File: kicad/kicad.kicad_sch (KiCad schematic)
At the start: 19 parts, among them J1 12V_IN, J2 MOTOR_POLOLU_3039, J3 NUCLEO_G0B1RE_IF, J4 CAN, Q1 IRLZ44NPBF, U1 TC4427ACPA, U2 INA180A1IDBVR, U3 TCAN332DR

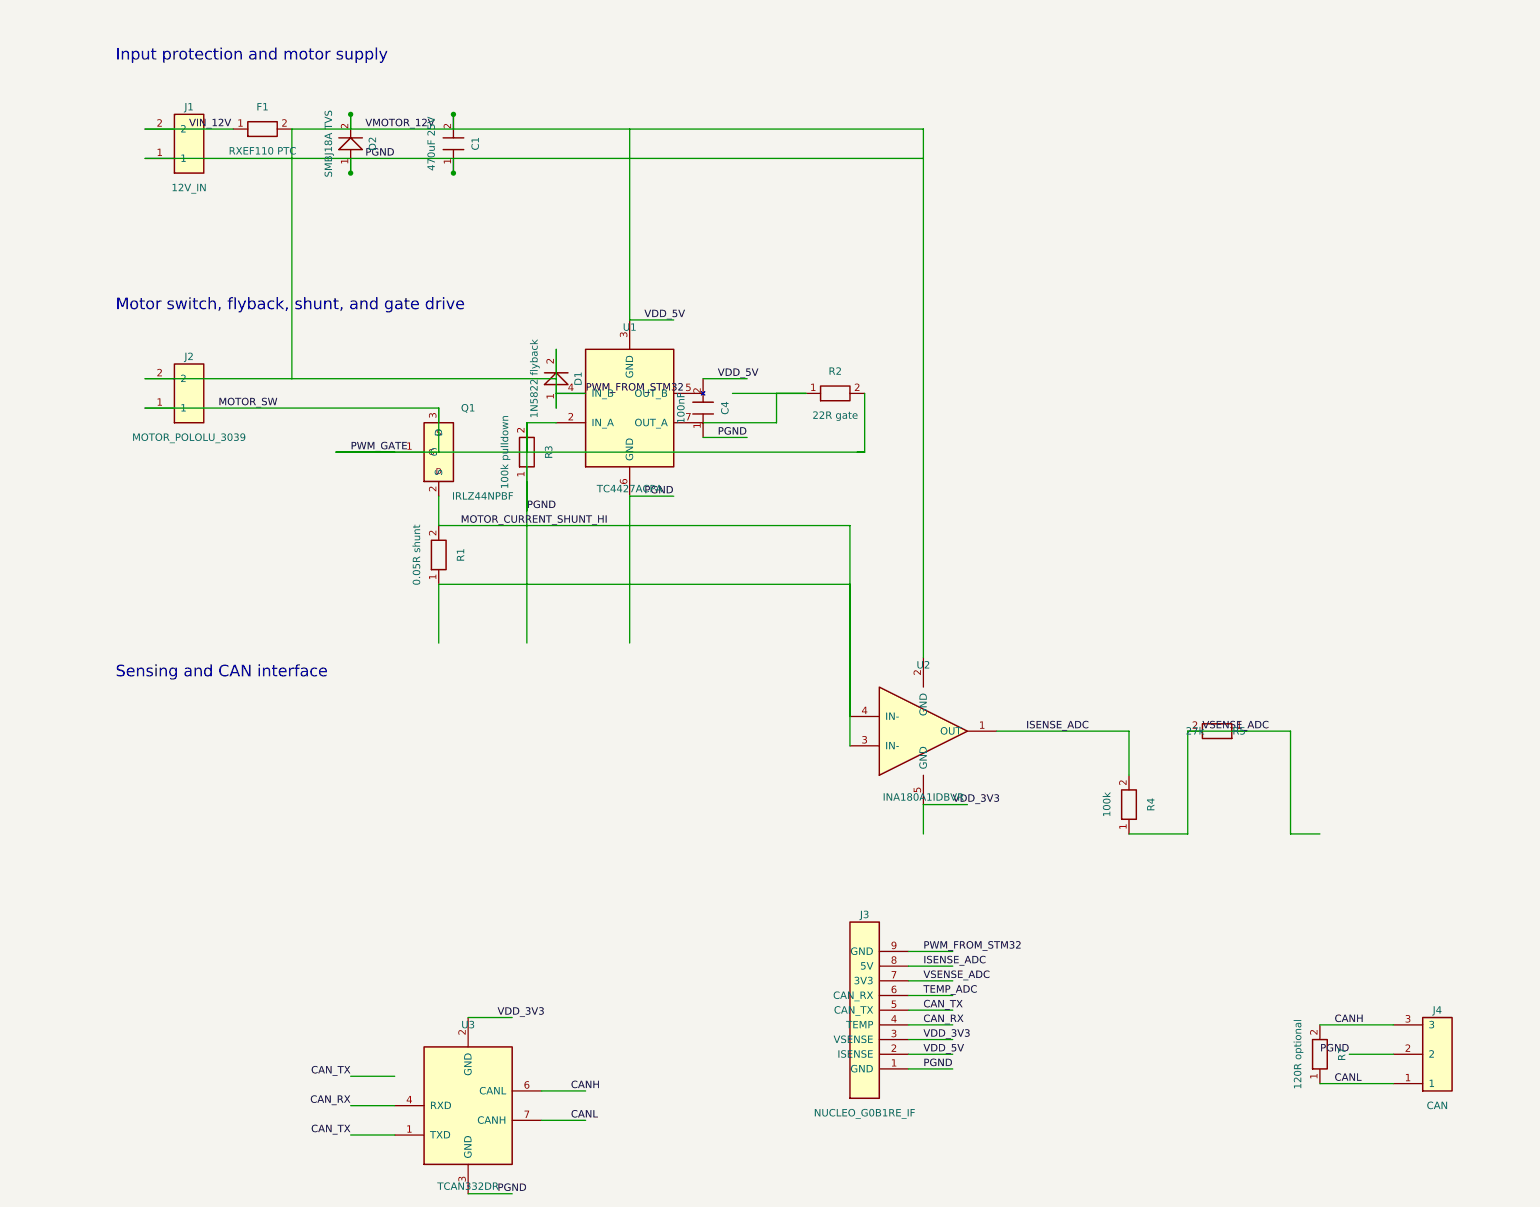
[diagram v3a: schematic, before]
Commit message: Finish schematic ERC cleanup
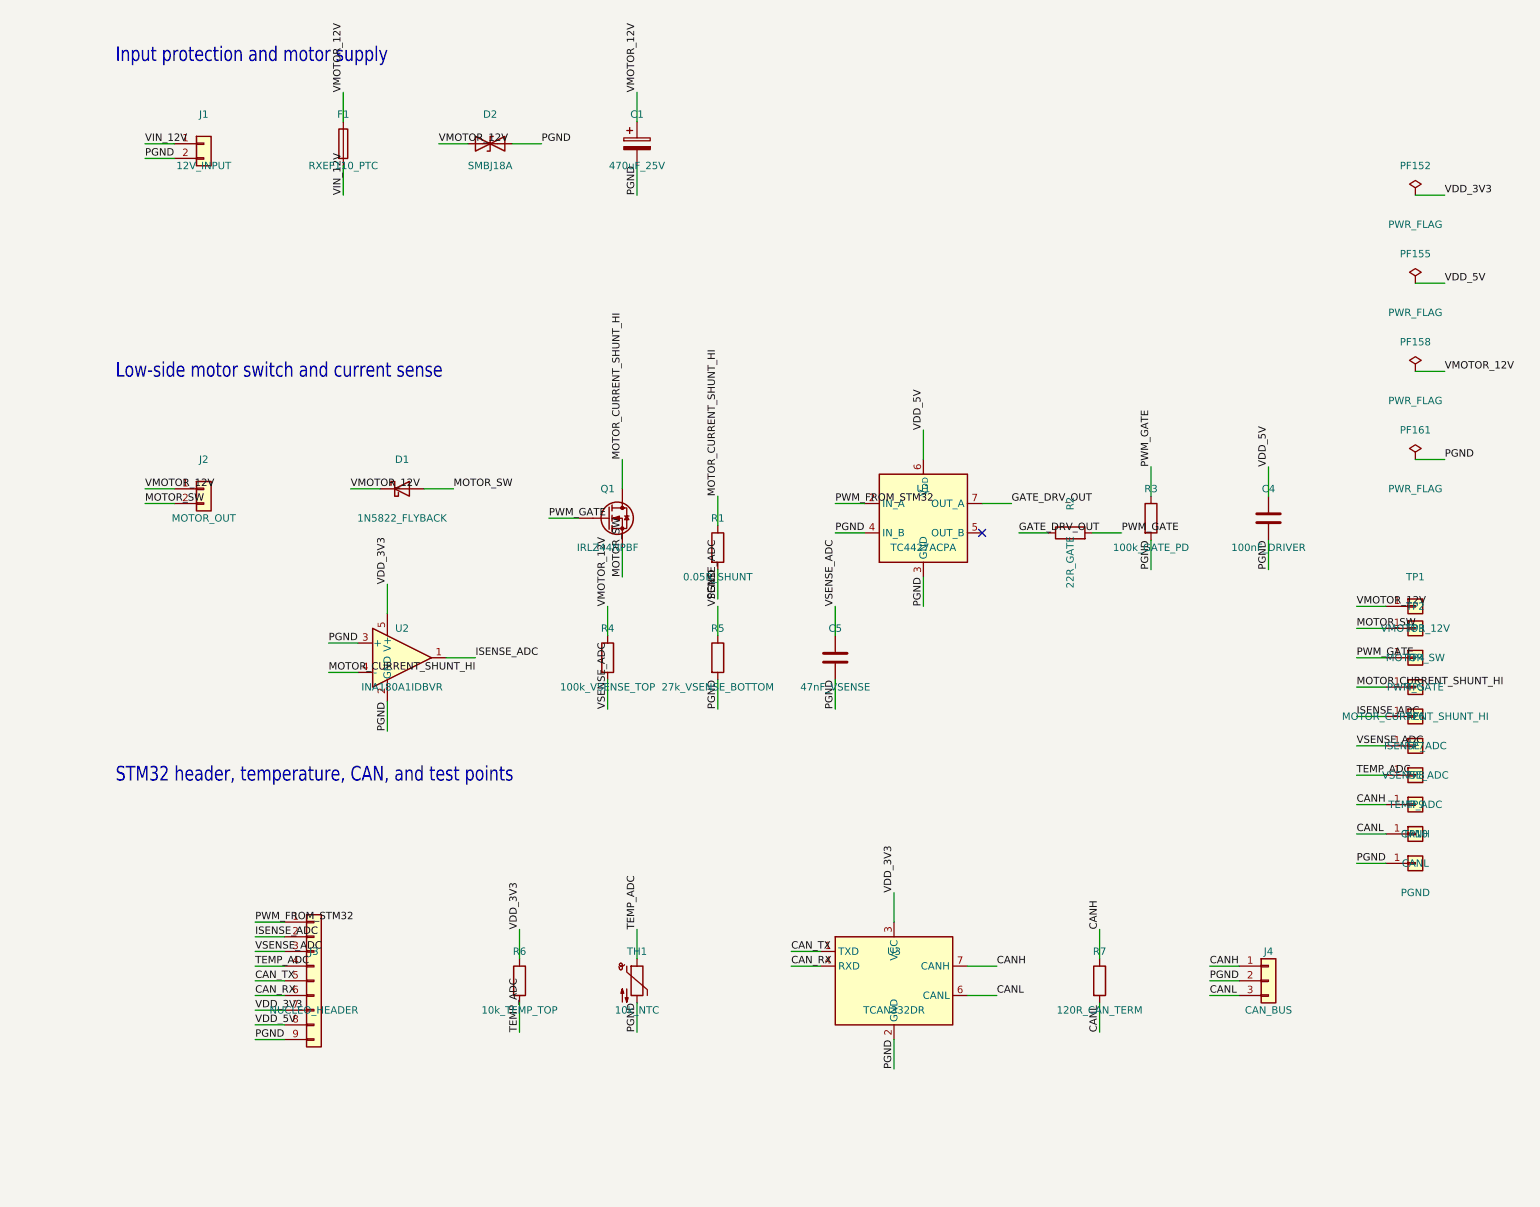
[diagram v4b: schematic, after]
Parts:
- removed C1: 470uF 25V, Capacitor_THT:CP_Radial_D8.0mm_P3.50mm, symbol V1:C_V
- removed C4: 100nF, Capacitor_SMD:C_0805_2012Metric, symbol V1:C_V
- removed D1: 1N5822 flyback, Diode_THT:D_DO-201AD_P15.24mm_Horizontal, symbol V1:DIODE_V
- removed D2: SMBJ18A TVS, Diode_SMD:D_SMB, symbol V1:DIODE_V
- removed F1: RXEF110 PTC, Fuse:Fuseholder5x20_horiz_open, symbol V1:R_H
- removed J1: 12V_IN, TerminalBlock:TerminalBlock_1x02_P5.00mm, symbol V1:CONN2
- removed J2: MOTOR_POLOLU_3039, TerminalBlock:TerminalBlock_1x02_P5.00mm, symbol V1:CONN2
- removed J3: NUCLEO_G0B1RE_IF, Connector_PinHeader_2.54mm:PinHeader_1x09_P2.54mm_Vertical, symbol V1:CONN9
- removed J4: CAN, TerminalBlock:TerminalBlock_1x03_P3.50mm, symbol V1:CONN3
- removed Q1: IRLZ44NPBF, Package_TO_SOT_THT:TO-220-3_Vertical, symbol V1:NMOS
- removed R1: 0.05R shunt, Resistor_SMD:R_2512_6332Metric, symbol V1:R_V
- removed R2: 22R gate, Resistor_SMD:R_0805_2012Metric, symbol V1:R_H
- removed R3: 100k pulldown, Resistor_SMD:R_0805_2012Metric, symbol V1:R_V
- removed R4: 100k, Resistor_SMD:R_0805_2012Metric, symbol V1:R_V
- removed R5: 27k, Resistor_SMD:R_0805_2012Metric, symbol V1:R_V
- removed R7: 120R optional, Resistor_SMD:R_0805_2012Metric, symbol V1:R_V
- removed U1: TC4427ACPA, Package_DIP:DIP-8_W7.62mm, symbol V1:GATE_DRIVER
- removed U2: INA180A1IDBVR, Package_TO_SOT_SMD:SOT-23-5, symbol V1:INA180
- removed U3: TCAN332DR, Package_SO:SOIC-8_3.9x4.9mm_P1.27mm, symbol V1:CAN
- added C1: 470uF_25V, Capacitor_THT:CP_Radial_D8.0mm_P3.50mm, symbol Device:C_Polarized
- added C4: 100nF_DRIVER, Capacitor_SMD:C_0805_2012Metric, symbol Device:C
- added C5: 47nF_VSENSE, Capacitor_SMD:C_0805_2012Metric, symbol Device:C
- added D1: 1N5822_FLYBACK, Diode_THT:D_DO-201AD_P15.24mm_Horizontal, symbol Device:D_Schottky
- added D2: SMBJ18A, Diode_SMD:D_SMB, symbol Device:D_TVS
- added F1: RXEF110_PTC, Fuse:Fuseholder_Clip-5x20mm_Littelfuse_111_Inline_P20.00x5.00mm_D1.05mm_Horizontal, symbol Device:Fuse
- added J1: 12V_INPUT, TerminalBlock:TerminalBlock_MaiXu_MX126-5.0-02P_1x02_P5.00mm, symbol Connector_Generic:Conn_01x02
- added J2: MOTOR_OUT, TerminalBlock:TerminalBlock_MaiXu_MX126-5.0-02P_1x02_P5.00mm, symbol Connector_Generic:Conn_01x02
- added J3: NUCLEO_HEADER, Connector_PinHeader_2.54mm:PinHeader_1x09_P2.54mm_Vertical, symbol Connector_Generic:Conn_01x09
- added J4: CAN_BUS, TerminalBlock:TerminalBlock_MaiXu_MX126-5.0-03P_1x03_P5.00mm, symbol Connector_Generic:Conn_01x03
- added Q1: IRLZ44NPBF, Package_TO_SOT_THT:TO-220-3_Vertical, symbol Device:Q_NMOS
- added R1: 0.05R_SHUNT, Resistor_SMD:R_2512_6332Metric, symbol Device:R
- added R2: 22R_GATE, Resistor_SMD:R_0805_2012Metric, symbol Device:R
- added R3: 100k_GATE_PD, Resistor_SMD:R_0805_2012Metric, symbol Device:R
- added R4: 100k_VSENSE_TOP, Resistor_SMD:R_0805_2012Metric, symbol Device:R
- added R5: 27k_VSENSE_BOTTOM, Resistor_SMD:R_0805_2012Metric, symbol Device:R
- added R6: 10k_TEMP_TOP, Resistor_SMD:R_0805_2012Metric, symbol Device:R
- added R7: 120R_CAN_TERM, Resistor_SMD:R_0805_2012Metric, symbol Device:R
- added TH1: 10k_NTC, Resistor_SMD:R_0805_2012Metric, symbol Device:Thermistor_NTC
- added TP1: VMOTOR_12V, TestPoint:TestPoint_Keystone_5000-5004_Miniature, symbol Connector_Generic:Conn_01x01
- added TP10: PGND, TestPoint:TestPoint_Keystone_5000-5004_Miniature, symbol Connector_Generic:Conn_01x01
- added TP2: MOTOR_SW, TestPoint:TestPoint_Keystone_5000-5004_Miniature, symbol Connector_Generic:Conn_01x01
- added TP3: PWM_GATE, TestPoint:TestPoint_Keystone_5000-5004_Miniature, symbol Connector_Generic:Conn_01x01
- added TP4: MOTOR_CURRENT_SHUNT_HI, TestPoint:TestPoint_Keystone_5000-5004_Miniature, symbol Connector_Generic:Conn_01x01
- added TP5: ISENSE_ADC, TestPoint:TestPoint_Keystone_5000-5004_Miniature, symbol Connector_Generic:Conn_01x01
- added TP6: VSENSE_ADC, TestPoint:TestPoint_Keystone_5000-5004_Miniature, symbol Connector_Generic:Conn_01x01
- added TP7: TEMP_ADC, TestPoint:TestPoint_Keystone_5000-5004_Miniature, symbol Connector_Generic:Conn_01x01
- added TP8: CANH, TestPoint:TestPoint_Keystone_5000-5004_Miniature, symbol Connector_Generic:Conn_01x01
- added TP9: CANL, TestPoint:TestPoint_Keystone_5000-5004_Miniature, symbol Connector_Generic:Conn_01x01
- added U1: TC4427ACPA, Package_DIP:DIP-8_W7.62mm, symbol Driver_FET:TC4427xOA
- added U2: INA180A1IDBVR, Package_TO_SOT_SMD:SOT-23-5, symbol Amplifier_Current:INA180A1
- added U3: TCAN332DR, Package_SO:SOIC-8_3.9x4.9mm_P1.27mm, symbol Interface_CAN_LIN:TCAN332
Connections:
- net CANH: now also J4.1 (Pin_1), R7.1, TP8.1 (Pin_1), U3.7 (CANH)
- net CANL: now also J4.3 (Pin_3), R7.2, TP9.1 (Pin_1), U3.6 (CANL)
- net CAN_RX: now also J3.6 (Pin_6), U3.4 (RXD)
- net CAN_TX: now also J3.5 (Pin_5), U3.1 (TXD)
- net ISENSE_ADC: now also J3.2 (Pin_2), TP5.1 (Pin_1), U2.1
- net MOTOR_CURRENT_SHUNT_HI: now also Q1.D, R1.1, TP4.1 (Pin_1), U2.4 (-)
- net MOTOR_SW: now also D1.2 (A), J2.2 (Pin_2), Q1.S, TP2.1 (Pin_1)
- net PGND: now also C1.2, C4.2, C5.2, D2.2 (A2), J1.2 (Pin_2), J3.9 (Pin_9), J4.2 (Pin_2), R1.2, R3.2, R5.2, TH1.2, TP10.1 (Pin_1), U1.3 (GND), U1.4 (IN_B), U2.2 (GND), U2.3 (+), U3.2 (GND)
- net PWM_FROM_STM32: now also J3.1 (Pin_1), U1.2 (IN_A)
- net PWM_GATE: now also Q1.G, R2.2, R3.1, TP3.1 (Pin_1)
- net TEMP_ADC: now also J3.4 (Pin_4), R6.2, TH1.1, TP7.1 (Pin_1)
- net VDD_3V3: now also J3.7 (Pin_7), R6.1, U2.5 (V+), U3.3 (VCC)
- net VDD_5V: now also C4.1, J3.8 (Pin_8), U1.6 (V_{DD})
- net VIN_12V: now also F1.2, J1.1 (Pin_1)
- net VMOTOR_12V: now also C1.1, D1.1 (K), D2.1 (A1), F1.1, J2.1 (Pin_1), R4.1, TP1.1 (Pin_1)
- net VSENSE_ADC: now also C5.1, J3.3 (Pin_3), R4.2, R5.1, TP6.1 (Pin_1)
- new net GATE_DRV_OUT: R2.1, U1.7 (OUT_A)
- no-connect marks 0 -> 1
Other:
- note added: "Low-side motor switch and current sense"
- note added: "STM32 header, temperature, CAN, and test points"
- note removed: "Motor switch, flyback, shunt, and gate drive"
- note removed: "Sensing and CAN interface"
